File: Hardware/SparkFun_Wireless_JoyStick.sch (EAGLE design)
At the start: 56 parts, among them J5 CORTEX_DEBUGPTH, Q2 2.5A/30V, U1 JOYSTICKPTH, U2 MCP73831, U3 AP2112K-3.3V, U4 JOYSTICKPTH, U6 ATSAMD21G-A, U7 74AHC1G125, Y2 32.768kHz

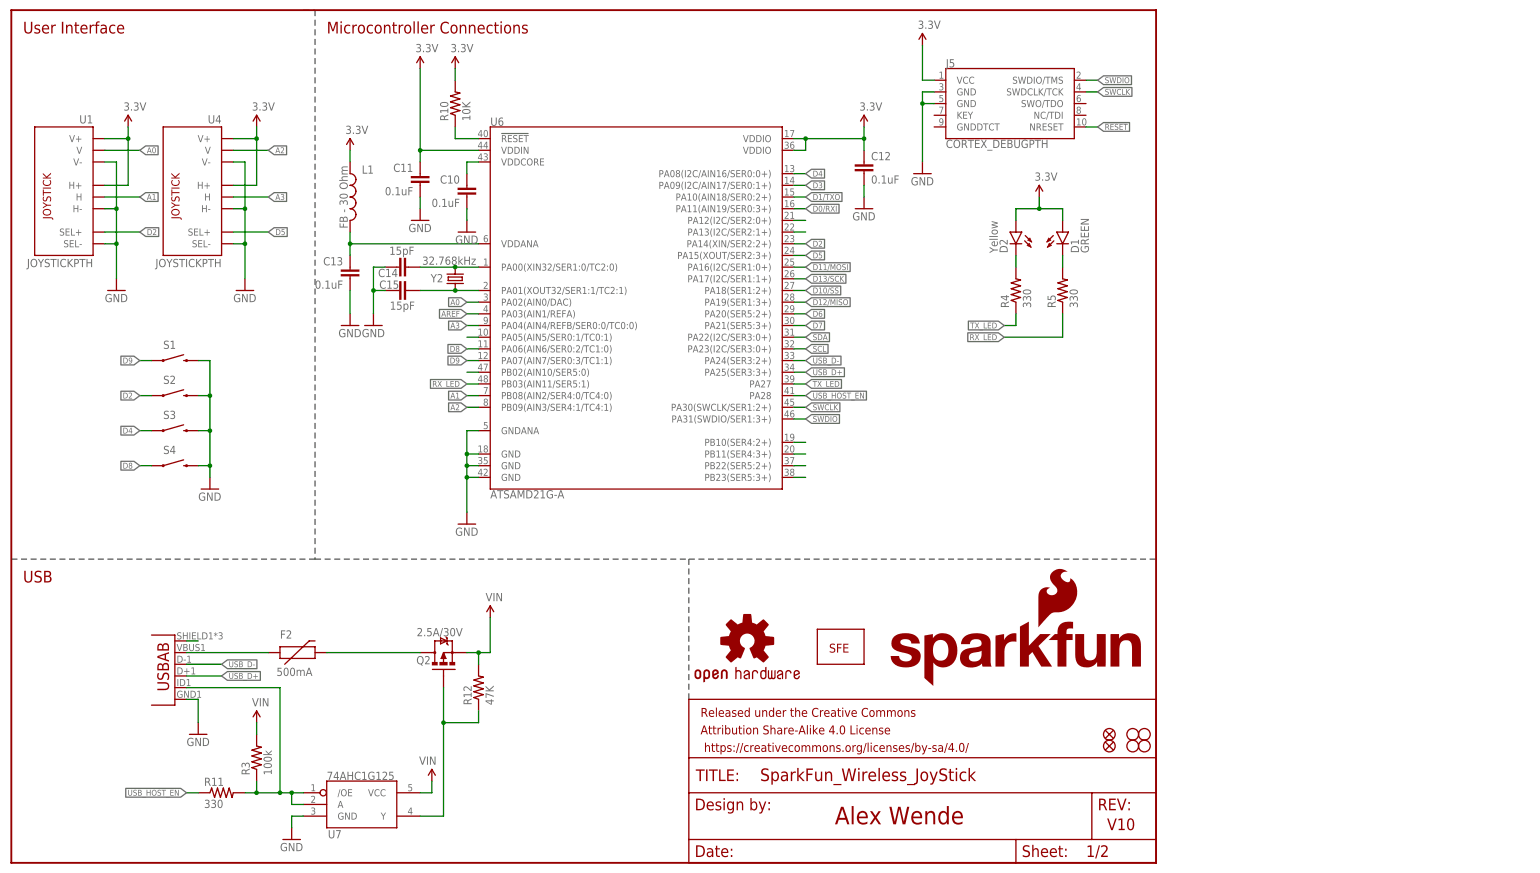
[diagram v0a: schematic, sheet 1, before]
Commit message: V10 Updates
- Broke out extra pins
- Added LiPo fuel gauge
- Added "trigger" buttons
- Cleaned up layout
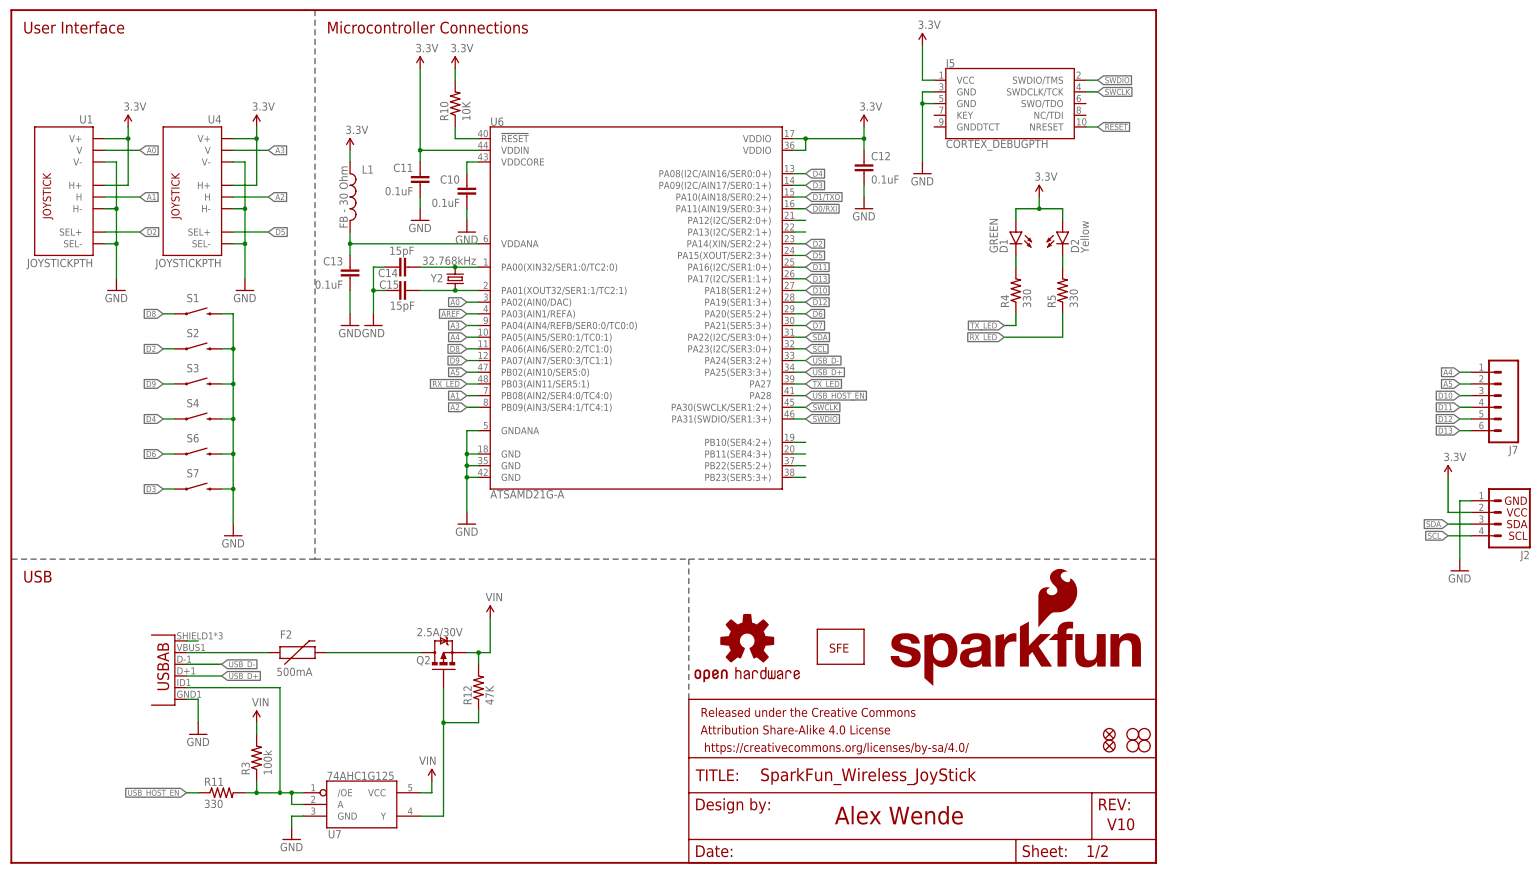
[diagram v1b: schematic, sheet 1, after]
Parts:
- added C1: 1.0uF, SparkFun-Capacitors:1.0UF-16V-10%(0603)
- added C2: 10nF, SparkFun-Capacitors:10NF/10000PF-50V-10%(0603)
- added J2: (no value), SparkFun-Connectors:I2C_STANDARD_NO_SILK
- added J7: (no value), SparkFun-Connectors:M06NO_SILK_FEMALE_PTH
- added R1: 1K, SparkFun-Resistors:1KOHM-1/10W-1%(0603)
- added R13, R14, R15: 4.7K, SparkFun-Resistors:4.7KOHM-1/10W-1%(0603)
- added R2: 180, SparkFun-Resistors:180OHM1/10W1%(0603)
- added S6, S7: SWITCH-MOMENTARY-2SIDE_EZ, SparkFun-Electromechanical:SWITCH-MOMENTARY-2SIDE_EZ
- added U5: MAX1704X, SparkFun-PowerIC:MAX1704X
- LOGO2: value SFE_LOGO_NAME_FLAME.2_INCH -> SFE_LOGO_NAME_FLAME.3_INCH; device SparkFun-Aesthetics:SFE_LOGO_NAME_FLAME.2_INCH -> SparkFun-Aesthetics:SFE_LOGO_NAME_FLAME.3_INCH
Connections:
- removed net D10/SS: U6.PA18(SER1:2+)
- removed net D11/MOSI: U6.PA16(I2C/SER1:0+)
- removed net D12/MISO: U6.PA19(SER1:3+)
- removed net D13/SCK: U6.PA17(I2C/SER1:1+)
- removed net N$11: D1.C, R5.2
- removed net N$29: U6.PB02(AIN10/SER5:0)
- removed net N$32: U6.PA05(AIN5/SER0:1/TC0:1)
- new net A4: J7.1, U6.PA05(AIN5/SER0:1/TC0:1)
- new net A5: J7.2, U6.PB02(AIN10/SER5:0)
- new net D10: J7.3, U6.PA18(SER1:2+)
- new net D11: J7.4, U6.PA16(I2C/SER1:0+)
- new net D12: J7.5, U6.PA19(SER1:3+)
- new net D13: J7.6, U6.PA17(I2C/SER1:1+)
- new net N$1: D2.C, R5.2
- new net N$10: D1.C, R4.2
- new net N$16: C1.1, R1.2, U5.CELL
- net 3.3V: now also J2.2, R13.1, R14.1, R15.1, R2.2
- net A2: now also U4.H; no longer U4.V
- net A3: now also U4.V; no longer U4.H
- net D3: now also S7.1
- net D4: now also S4.1; no longer S3.1
- net D6: now also S6.1
- net D7: now also R15.2, U5.ALT
- net D8: now also S1.1; no longer S4.1
- net D9: now also S3.1; no longer S1.1
- net GND: now also C1.2, C2.2, J2.1, S6.2, S7.2, U5.CTG, U5.GND@4, U5.GND@EP, U5.QST
- net N$12: now also C2.1, R2.1, U5.VDD; no longer D2.C, R4.2
- net SCL: now also J2.4, R14.2, U5.SCL
- net SDA: now also J2.3, R13.2, U5.SDA
- net VBAT: now also R1.1
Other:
- moved on the sheet: D1, D2, S1, S2, S3, S4

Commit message: V10 update
- Broke out a few more pins
- Cleaned up the schematic
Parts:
- removed U$1: SFE_LOGO_NAME_WEB, SparkFun-Aesthetics:SFE_LOGO_NAME_WEB
- added J1: (no value), SparkFun-Connectors:M06NO_SILK_FEMALE_PTH
- added JP4: JUMPER-PAD-3-NC_BY_PASTE, SparkFun-Passives:JUMPER-PAD-3-NC_BY_PASTE
- D4: value RED -> BLUE; device SparkFun-LED:LED-RED0603 -> SparkFun-LED:LED-BLUE0603
- JP1: value JUMPER-PAD-3-2OF3_NC_BY_TRACE_SMALL -> JUMPER-PAD-3-2OF3_NC_BY_PASTE; device SparkFun-Passives:JUMPER-PAD-3-2OF3_NC_BY_TRACE_SMALL -> SparkFun-Passives:JUMPER-PAD-3-2OF3_NC_BY_PASTE
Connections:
- removed net N$13: R10.1, U6.!RESET!
- removed net N$7: U6.PA12(I2C/SER2:0+)
- new net SPI_MISO: J1.6, U6.PA12(I2C/SER2:0+)
- new net SPI_MOSI: J1.4, U6.PB10(SER4:2+)
- new net SPI_SCK: J1.5, U6.PB11(SER4:3+)
- net !RESET: now also R10.1, U6.!RESET!
- net 3.3V: now also J1.1, JP4.2; no longer R13.1, R14.1
- net GND: now also J1.2, J1.3
- net N$2: now also JP4.1, R14.1; no longer U6.PB10(SER4:2+)
- net N$3: now also JP4.3, R13.1; no longer U6.PB11(SER4:3+)
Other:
- note added: "DOWN"
- note added: "IO Connections"
- note added: "LEFT"
- note added: "LEFT TRIG"
- note added: "Left Joystick"
- note added: "LiPo Fuel Gauge"
- note added: "RIGHT"
- note added: "RIGHT TRIG"
- note added: "R_PROG = kOhms I_REG = milliamperes I_REG = 500mA MAX"
- note added: "Right Joystick"
- note added: "UP"
- note added: "XBee Socket"
- note removed: "R_PROG = kOhms I_REG = milliamperes"
- note removed: "XBee"

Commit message: V10 Updates
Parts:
- removed C13: 0.1uF, SparkFun-Capacitors:0.1UF-25V(+80/-20%)(0603)
- removed C15: 15pF, SparkFun-Capacitors:15PF-50V-5%(0603)
- removed JP3: (no value), SparkFun-Connectors:USB-ABCONN-11794
- removed JP4: JUMPER-PAD-3-NC_BY_PASTE, SparkFun-Passives:JUMPER-PAD-3-NC_BY_PASTE
- added C3: 4.7uF, SparkFun-Capacitors:4.7UF-6.3V-10%(0603)0603
- added C4: 1.0uF, SparkFun-Capacitors:1.0UF-16V-10%(0603)
- added J6: (no value), SparkFun-Connectors:M021X02_NO_SILK
- added TP1: TEST-POINT3, SparkFun-Passives:TEST-POINT3
- added U8: ATSAMD21G-A, SparkFun-DigitalIC:ATSAMD21G-A
- C1: device SparkFun-Capacitors:1.0UF-16V-10%(0603) -> SparkFun-Capacitors:1.0UF-25V-+80/-20(0805)"
- C10: value 0.1uF -> 15pF; device SparkFun-Capacitors:0.1UF-25V(+80/-20%)(0603) -> SparkFun-Capacitors:15PF-50V-5%(0603)
- C2: value 10nF -> 2.2uF; device SparkFun-Capacitors:10NF/10000PF-50V-10%(0603) -> SparkFun-Capacitors:2.2UF-10V-20%(0603)
- C5: value 4.7uF -> 10nF; device SparkFun-Capacitors:4.7UF-6.3V-10%(0603)0603 -> SparkFun-Capacitors:10NF/10000PF-50V-10%(0603)
- C7: value 1.0uF -> 0.1uF; device SparkFun-Capacitors:1.0UF-25V-+80/-20(0805)" -> SparkFun-Capacitors:0.1UF-25V(+80/-20%)(0603)
- C8: value 2.2uF -> 0.1uF; device SparkFun-Capacitors:2.2UF-10V-20%(0603) -> SparkFun-Capacitors:0.1UF-25V(+80/-20%)(0603)
- D1: value GREEN -> RED; device SparkFun-LED:LED-GREEN0603 -> SparkFun-LED:LED-RED0603
- D2: value Yellow -> BLUE; device SparkFun-LED:LED-YELLOW0603 -> SparkFun-LED:LED-BLUE0603
- D3: value RED -> GREEN; device SparkFun-LED:LED-RED0603 -> SparkFun-LED:LED-GREEN0603
- D4: value BLUE -> Yellow; device SparkFun-LED:LED-BLUE0603 -> SparkFun-LED:LED-YELLOW0603
- J1: device SparkFun-Connectors:M06NO_SILK_FEMALE_PTH -> SparkFun-Connectors:USB-ABCONN-11794
- J2: device SparkFun-Connectors:I2C_STANDARD_NO_SILK -> SparkFun-Connectors:M06NO_SILK_FEMALE_PTH
- J3: device SparkFun-Connectors:JST_2MM_MALE -> SparkFun-Connectors:M06NO_SILK_FEMALE_PTH
- J4: device SparkFun-Connectors:M021X02_NO_SILK -> SparkFun-Connectors:I2C_STANDARD_NO_SILK
- J5: value CORTEX_DEBUGPTH -> (none); device SparkFun-Connectors:CORTEX_DEBUGPTH -> SparkFun-Connectors:JST_2MM_MALE
- J7: value (none) -> CORTEX_DEBUGPTH; device SparkFun-Connectors:M06NO_SILK_FEMALE_PTH -> SparkFun-Connectors:CORTEX_DEBUGPTH
- JP2: value (none) -> JUMPER-PAD-3-NC_BY_PASTE; device SparkFun-RF:XBEE-1B1 -> SparkFun-Passives:JUMPER-PAD-3-NC_BY_PASTE
- LOGO1: value OSHW-LOGOL -> SFE_LOGO_NAME_FLAME.3_INCH; device SparkFun-Aesthetics:OSHW-LOGOL -> SparkFun-Aesthetics:SFE_LOGO_NAME_FLAME.3_INCH
- LOGO2: value SFE_LOGO_NAME_FLAME.3_INCH -> OSHW-LOGOL; device SparkFun-Aesthetics:SFE_LOGO_NAME_FLAME.3_INCH -> SparkFun-Aesthetics:OSHW-LOGOL
- R1: value 1K -> 100k; device SparkFun-Resistors:1KOHM-1/10W-1%(0603) -> SparkFun-Resistors:100KOHM-1/10W-1%(0603)
- R10: value 10K -> 4.7K; device SparkFun-Resistors:10KOHM-1/10W-1%(0603)0603 -> SparkFun-Resistors:4.7KOHM-1/10W-1%(0603)
- R11: value 330 -> 4.7K; device SparkFun-Resistors:330OHM1/10W1%(0603) -> SparkFun-Resistors:4.7KOHM-1/10W-1%(0603)
- R12: value 47K -> 4.7K; device SparkFun-Resistors:47KOHM1/10W1%(0603) -> SparkFun-Resistors:4.7KOHM-1/10W-1%(0603)
- R13: value 4.7K -> 10K; device SparkFun-Resistors:4.7KOHM-1/10W-1%(0603) -> SparkFun-Resistors:10KOHM-1/10W-1%(0603)0603
- R14, R15: value 4.7K -> 330; device SparkFun-Resistors:4.7KOHM-1/10W-1%(0603) -> SparkFun-Resistors:330OHM1/10W1%(0603)
- R2: value 180 -> 330; device SparkFun-Resistors:180OHM1/10W1%(0603) -> SparkFun-Resistors:330OHM1/10W1%(0603)
- R3: value 100k -> 47K; device SparkFun-Resistors:100KOHM-1/10W-1%(0603) -> SparkFun-Resistors:47KOHM1/10W1%(0603)
- R4: value 330 -> 470; device SparkFun-Resistors:330OHM1/10W1%(0603) -> SparkFun-Resistors:470OHM1/10W1%(0603)
- R5: value 330 -> 1K; device SparkFun-Resistors:330OHM1/10W1%(0603) -> SparkFun-Resistors:1KOHM-1/10W-1%(0603)
- R7: value 2.0k -> 180; device SparkFun-Resistors:2.0KOHM1/10W5%(0603) -> SparkFun-Resistors:180OHM1/10W1%(0603)
- R8: value R_PROG -> 2.0k; device SparkFun-Resistors:RESISTORPTH-1/4W -> SparkFun-Resistors:2.0KOHM1/10W5%(0603)
- R9: value 470 -> R_PROG; device SparkFun-Resistors:470OHM1/10W1%(0603) -> SparkFun-Resistors:RESISTORPTH-1/4W
- S5: value SWITCH_SPDT -> SWITCH-MOMENTARY-2SIDE_EZ; device SparkFun-Electromechanical:SWITCH_SPDT -> SparkFun-Electromechanical:SWITCH-MOMENTARY-2SIDE_EZ
- S7: value SWITCH-MOMENTARY-2SIDE_EZ -> SWITCH_SPDT; device SparkFun-Electromechanical:SWITCH-MOMENTARY-2SIDE_EZ -> SparkFun-Electromechanical:SWITCH_SPDT
- U2: value MCP73831 -> JOYSTICKPTH; device SparkFun-PowerIC:MCP73831 -> SparkFun-Electromechanical:JOYSTICKPTH
- U3: value AP2112K-3.3V -> 74AHC1G125; device SparkFun-PowerIC:V_REG_LDOSMD -> SparkFun-DigitalIC:74AHC1G125; PROD_ID VREG-12457 -> (none)
- U4: value JOYSTICKPTH -> AP2112K-3.3V; device SparkFun-Electromechanical:JOYSTICKPTH -> SparkFun-PowerIC:V_REG_LDOSMD; PROD_ID (none) -> VREG-12457
- U5: value MAX1704X -> XBEE-2B3; device SparkFun-PowerIC:MAX1704X -> SparkFun-RF:XBEE-2B3
- U6: value ATSAMD21G-A -> MAX1704X; device SparkFun-DigitalIC:ATSAMD21G-A -> SparkFun-PowerIC:MAX1704X
- U7: value 74AHC1G125 -> MCP73831; device SparkFun-DigitalIC:74AHC1G125 -> SparkFun-PowerIC:MCP73831
- renumbered C14 to C9, F2 to F1, Q2 to Q1, Y2 to Y1
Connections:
- net !RESET: now also J7.NRESET, R13.1, U8.!RESET!; no longer J5.NRESET, R10.1, U6.!RESET!
- net 3.3V: now also C2.1, D3.A, D4.A, J2.1, J4.2, J7.VCC, JP2.2, R12.1, R13.2, R4.2, R7.2, U2.H+, U2.V+, U4.OUT, U5.VDD, U8.VDDIN, U8.VDDIO@17, U8.VDDIO@36; no longer C11.1, D1.A, D2.A, J1.1, J2.2, J5.VCC, JP2.VDD, JP4.2, R10.2, R15.1, R2.2, R9.2, U3.OUT, U4.H+, U4.V+, U6.VDDIN, U6.VDDIO@17, U6.VDDIO@36
- net A0: now also U2.V, U8.PA02(AIN0/DAC); no longer U1.V, U6.PA02(AIN0/DAC)
- net A1: now also U2.H, U8.PB08(AIN2/SER4:0/TC4:0); no longer U1.H, U6.PB08(AIN2/SER4:0/TC4:0)
- net A2: now also U1.H, U8.PB09(AIN3/SER4:1/TC4:1); no longer U4.H, U6.PB09(AIN3/SER4:1/TC4:1)
- net A3: now also U1.V, U8.PA04(AIN4/REFB/SER0:0/TC0:0); no longer U4.V, U6.PA04(AIN4/REFB/SER0:0/TC0:0)
- net A4: now also J3.1, U8.PA05(AIN5/SER0:1/TC0:1); no longer J7.1, U6.PA05(AIN5/SER0:1/TC0:1)
- net A5: now also J3.2, U8.PB02(AIN10/SER5:0); no longer J7.2, U6.PB02(AIN10/SER5:0)
- net AREF: now also TP1.1, U8.PA03(AIN1/REFA); no longer U6.PA03(AIN1/REFA)
- net D0/RXI: now also U5.DOUT, U8.PA11(AIN19/SER0:3+); no longer JP2.DOUT, U6.PA11(AIN19/SER0:3+)
- net D1/TXO: now also U5.DIN, U8.PA10(AIN18/SER0:2+); no longer JP2.DIN, U6.PA10(AIN18/SER0:2+)
- net D10: now also J3.3, U8.PA18(SER1:2+); no longer J7.3, U6.PA18(SER1:2+)
- net D11: now also J3.4, U8.PA16(I2C/SER1:0+); no longer J7.4, U6.PA16(I2C/SER1:0+)
- net D12: now also J3.5, U8.PA19(SER1:3+); no longer J7.5, U6.PA19(SER1:3+)
- net D13: now also J3.6, U8.PA17(I2C/SER1:1+); no longer J7.6, U6.PA17(I2C/SER1:1+)
- net D2: now also U2.SEL+, U8.PA14(XIN/SER2:2+); no longer U1.SEL+, U6.PA14(XIN/SER2:2+)
- net D3: now also S6.1, U8.PA09(I2C/AIN17/SER0:1+); no longer S7.1, U6.PA09(I2C/AIN17/SER0:1+)
- net D4: now also U8.PA08(I2C/AIN16/SER0:0+); no longer U6.PA08(I2C/AIN16/SER0:0+)
- net D5: now also U1.SEL+, U8.PA15(XOUT/SER2:3+); no longer U4.SEL+, U6.PA15(XOUT/SER2:3+)
- net D6: now also S5.1, U8.PA20(SER5:2+); no longer S6.1, U6.PA20(SER5:2+)
- net D7: now also R12.2, U6.ALT, U8.PA21(SER5:3+); no longer R15.2, U5.ALT, U6.PA21(SER5:3+)
- net D8: now also U8.PA06(AIN6/SER0:2/TC1:0); no longer U6.PA06(AIN6/SER0:2/TC1:0)
- net D9: now also U8.PA07(AIN7/SER0:3/TC1:1); no longer U6.PA07(AIN7/SER0:3/TC1:1)
- net GND: now also C10.1, C3.2, C4.2, D1.C, J1.GND, J2.2, J2.3, J5.-, J6.1, J7.GND@3, J7.GND@5, R9.1, S5.2, U2.H-, U2.SEL-, U2.V-, U4.GND, U5.GND, U6.CTG, U6.GND@4, U6.GND@EP, U6.QST, U7.VSS, U8.GND@18, U8.GND@35, U8.GND@42, U8.GNDANA; no longer C10.2, C13.2, C15.1, D4.C, J1.2, J1.3, J2.1, J3.-, J5.GND@3, J5.GND@5, JP2.GND, JP3.GND, R7.1, S7.2, U2.VSS, U4.H-, U4.SEL-, U4.V-, U5.CTG, U5.GND@4, U5.GND@EP, U5.QST, U6.GND@18, U6.GND@35, U6.GND@42, U6.GNDANA, U7.GND
- net N$1: now also D4.C, R15.2; no longer D2.C, R5.2
- net N$10: now also D3.C, R14.2; no longer D1.C, R4.2
- net N$12: now also C5.1, R7.1, U6.VDD; no longer C2.1, R2.1, U5.VDD
- net N$15: now also J1.USBID, R1.1, R2.2, U3./OE, U3.A; no longer JP3.USBID, R11.2, R3.1, U7./OE, U7.A
- net N$16: now also C4.1, R5.2, U6.CELL; no longer C1.1, R1.2, U5.CELL
- net N$17: now also R8.2; no longer R7.2
- net N$18: now also C11.1, U8.VDDCORE; no longer C10.1, U6.VDDCORE
- net N$19: now also D2.A; no longer D3.A
- net N$2: now also JP2.1, R11.1; no longer JP4.1, R14.1
- net N$20: now also D2.C, U7.STAT; no longer D3.C, U2.STAT
- net N$21: now also U8.PA00(XIN32/SER1:0/TC2:0); no longer U6.PA00(XIN32/SER1:0/TC2:0)
- net N$22: now also C10.2, U8.PA01(XOUT32/SER1:1/TC2:1); no longer C15.2, U6.PA01(XOUT32/SER1:1/TC2:1)
- net N$23: now also D1.A, R4.1; no longer D4.A, R9.1
- net N$24: now also C7.1, U8.VDDANA; no longer C13.1, U6.VDDANA
- net N$25: now also R3.1, U3.Y; no longer R12.1, U7.Y
- net N$3: now also JP2.3, R10.1; no longer JP4.3, R13.1
- net N$4: now also R9.2; no longer R8.2
- net N$5: now also U8.PB22(SER5:2+); no longer U6.PB22(SER5:2+)
- net N$6: now also U8.PB23(SER5:3+); no longer U6.PB23(SER5:3+)
- net N$8: now also U8.PA13(I2C/SER2:1+); no longer U6.PA13(I2C/SER2:1+)
- net N$9: now also J1.VBUS; no longer JP3.VBUS
- net PROG: now also U7.PROG; no longer U2.PROG
- net RX_LED: now also R15.1, U8.PB03(AIN11/SER5:1); no longer R5.1, U6.PB03(AIN11/SER5:1)
- net SCL: now also J4.4, R11.2, U6.SCL, U8.PA23(I2C/SER3:0+); no longer J2.4, R14.2, U5.SCL, U6.PA23(I2C/SER3:0+)
- net SDA: now also J4.3, R10.2, U6.SDA, U8.PA22(I2C/SER3:0+); no longer J2.3, R13.2, U5.SDA, U6.PA22(I2C/SER3:0+)
- net SHIELD: now also J1.SHIELD; no longer JP3.SHIELD
- net SPI_MISO: now also J2.6, U8.PA12(I2C/SER2:0+); no longer J1.6, U6.PA12(I2C/SER2:0+)
- net SPI_MOSI: now also J2.4, U8.PB10(SER4:2+); no longer J1.4, U6.PB10(SER4:2+)
- net SPI_SCK: now also J2.5, U8.PB11(SER4:3+); no longer J1.5, U6.PB11(SER4:3+)
- net SWCLK: now also J7.SWDCLK/TCK, U8.PA30(SWCLK/SER1:2+); no longer J5.SWDCLK/TCK, U6.PA30(SWCLK/SER1:2+)
- net SWDIO: now also J7.SWDIO/TMS, U8.PA31(SWDIO/SER1:3+); no longer J5.SWDIO/TMS, U6.PA31(SWDIO/SER1:3+)
- net TX_LED: now also R14.1, U8.PA27; no longer R4.1, U6.PA27
- net USB_D+: now also J1.D+, U8.PA25(SER3:3+); no longer JP3.D+, U6.PA25(SER3:3+)
- net USB_D-: now also J1.D-, U8.PA24(SER3:2+); no longer JP3.D-, U6.PA24(SER3:2+)
- net USB_HOST_EN: now also R2.1, U8.PA28; no longer R11.1, U6.PA28
- net VBAT: now also J5.+, J6.2, R5.1, S7.P, U7.VBAT; no longer J3.+, J4.2, R1.1, S5.P, U2.VBAT
- net VBAT_SW: now also C1.1, S7.O, U4.EN, U4.IN; no longer C7.1, S5.O, U3.EN, U3.IN
- net VIN: now also C3.1, R1.2, U3.VCC, U7.VIN; no longer C5.1, R12.2, U2.VIN, U7.VCC

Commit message: Design Review Changes
- Added LED to D13 for low batt indication.
- Added test points for bootloader programming from testbed
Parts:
- added D5: RED, SparkFun-LED:LED-RED0603
- added R16: 470, SparkFun-Resistors:470OHM1/10W1%(0603)
- added TP2, TP3, TP4: TEST-POINT3, SparkFun-Passives:TEST-POINT3
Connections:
- new net N$7: D5.A, R16.1
- net !RESET: now also TP4.1
- net D13: now also R16.2
- net GND: now also D5.C
- net SWCLK: now also TP3.1
- net SWDIO: now also TP2.1
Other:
- note added: "Charge Current Select"
- note added: "I2C Pullup"
- note added: "JTAG Programmer"
- note added: "LEDS"
- note added: "SAMD21"
- note added: "Test Points"
- note removed: "Microcontroller Connections"
- moved on the sheet: C10, C11, C12, C7, C8, C9, D3, D4, J7, L1, R13, R14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
